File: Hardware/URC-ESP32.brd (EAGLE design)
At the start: 120 x 54 mm, 94 parts, among them IC1 MCP9808-MSOP8, IC2 ESPWROOM32, IC3 LM358D, IC4 W5500-LQFP, IC5 CP2102N-A01-GQFN24, J1 SPI-LCD, J10 microSD, J2 I2CBR, J3 USB-C-16P-16P, J4 DC IN, J6 PWR_LED, Q1 FDN340P, Q2 MMDT3904, U1 HY931147C-RJ45

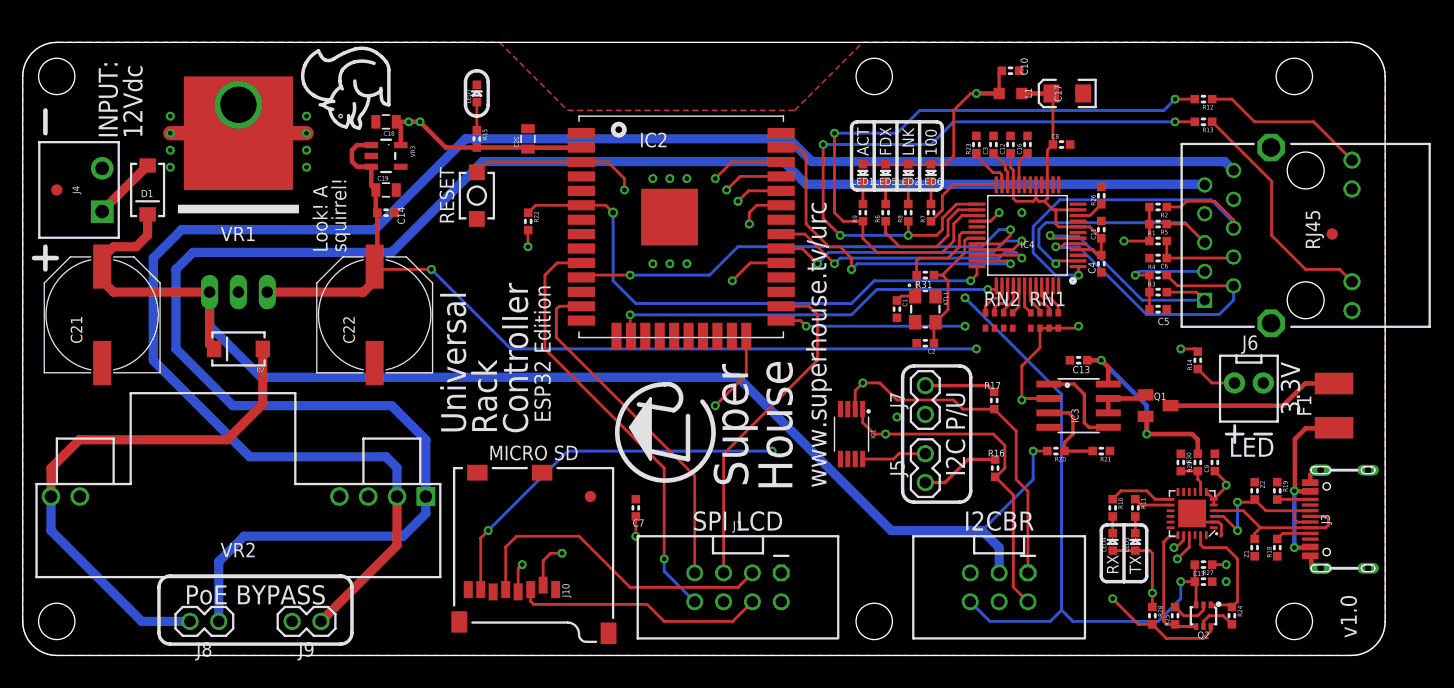
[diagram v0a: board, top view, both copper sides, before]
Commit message: Added I/O header with spare pins for I2C port 2 and serial port 2.
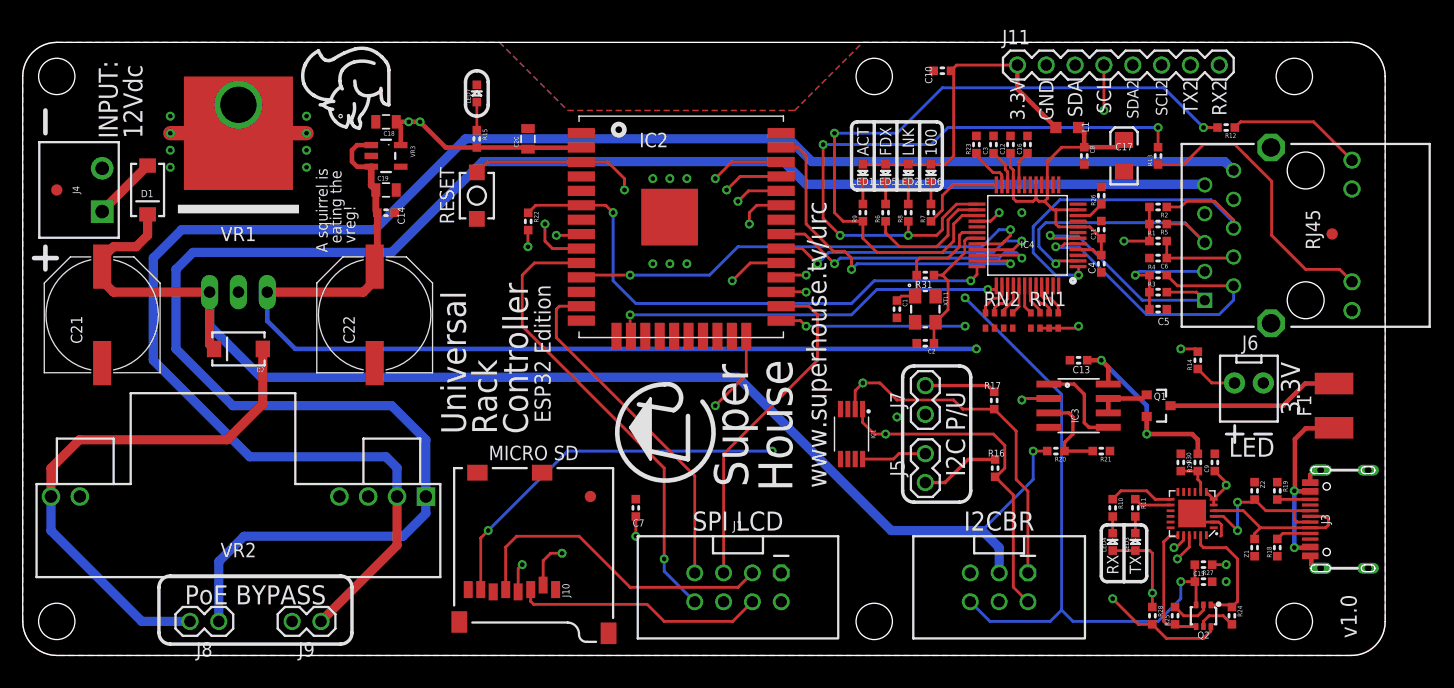
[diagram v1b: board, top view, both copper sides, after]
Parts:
- added J11: IO, SuperHouse-Connectors:1X08
- C1, C10, C11, C12, C13, C14, C15, C16, C2, C3, C4, C5, C6, C7, C8, C9: device SuperHouse-DiscreteSemi:C0603 -> SuperHouse-Capacitors:C0603
- C17: device SuperHouse-DiscreteSemi:EIA3216 -> SuperHouse-Capacitors:EIA3216
- C20: device SuperHouse-DiscreteSemi:C0805 -> SuperHouse-Capacitors:C0805
- D1, D2: device SuperHouse-DiscreteSemi:SMA-DIODE -> SuperHouse-Diodes:SMA-DIODE
- Q1: device freetronics-master-v1:SOT23 -> SuperHouse-Transistors:SOT23-3
- Q2: device SuperHouse-DiscreteSemi:SOT-363 -> SuperHouse-Transistors:SOT-363
- R1, R10, R11, R14, R15, R16, R17, R18, R19, R22, R23, R24, R25, R26, R27, R28, R29, R30, R31: device SuperHouse-DiscreteSemi:R0603 -> SuperHouse-Resistors:R0603
- RN1, RN2: device SuperHouse-DiscreteSemi:CAY16 -> SuperHouse-Resistors:CAY16
- Z1, Z2: device SuperHouse-DiscreteSemi:TVS0603 -> SuperHouse-Diodes:TVS0603
- moved C17 7.43 mm to (97.0, 44.0), turned to 90 degrees
- moved C10 6.00 mm to (81.0, 51.5), turned to 180 degrees
- moved L1 5.83 mm to (92.0, 46.5)
- moved R13 5.00 mm to (100.0, 44.0), turned to 90 degrees
- moved R12 3.20 mm to (106.0, 46.5)
- moved C8 2.24 mm to (93.5, 44.0), turned to 270 degrees
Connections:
- net IO27 renamed IO27_T7
- removed net IO16: IC2.27
- removed net IO17: IC2.28
- removed net IO32: IC2.8
- removed net IO33: IC2.9
- new net IO16_RX2: IC2.27, J11.8
- new net IO17_TX2: IC2.28, J11.7
- new net IO32_SCL2: IC2.8, J11.6
- new net IO33_SDA2: IC2.9, J11.5
- net 3.3V: now also J11.1
- net GND: now also J11.2
- net IO21_SDA: now also J11.3
- net IO22_SCL: now also J11.4
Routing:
- net IO33_SDA2: track 0.00 -> 63.7 mm, vias 0 -> 1
- net IO32_SCL2: track 0.00 -> 63.5 mm, vias 0 -> 1
- net IO16_RX2: track 0.00 -> 52.3 mm, vias 0 -> 1
- net IO17_TX2: track 0.00 -> 49.3 mm, vias 0 -> 1
- net IO22_SCL: track 64.3 -> 105.0 mm, vias 2 -> 3
- net IO21_SDA: track 57.5 -> 95.6 mm
- net 5V: track 111.7 -> 121.7 mm, vias 4 -> 3
- net N$332: track 20.9 -> 25.6 mm
- net ACTLED: track 57.1 -> 60.9 mm
- net 3.3V: track 86.5 -> 89.3 mm, vias 14 -> 13
- net IO25_TFT_CS: track 37.9 -> 40.7 mm
- net N$67: track 14.5 -> 11.9 mm
- net LINKLED: track 57.2 -> 55.5 mm
- net 3V3A: track 33.6 -> 34.2 mm
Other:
- board text added: "A squirrel is eating the vreg!"
- board text added: "IO16_RX2"
- board text added: "IO17_TX2"
- board text added: "IO21_SDA"
- board text added: "IO22_SCL"
- board text added: "IO32_SCL2"
- board text added: "IO33_SDA2"
- board text added: "RX2"
- board text added: "SCL2"
- board text added: "SDA2"
- board text added: "TX2"
- board text removed: "Look! A squirrel!"
